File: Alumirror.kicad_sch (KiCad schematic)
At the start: 26 parts, among them J1 USB_C_Receptacle_USB2.0_16P_2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, J3 USB_C_Receptacle_USB2.0_16P_2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, SW10 BOOT, U1 CH552T, U3 USBLC6-2P6, U5 USBLC6-2P6

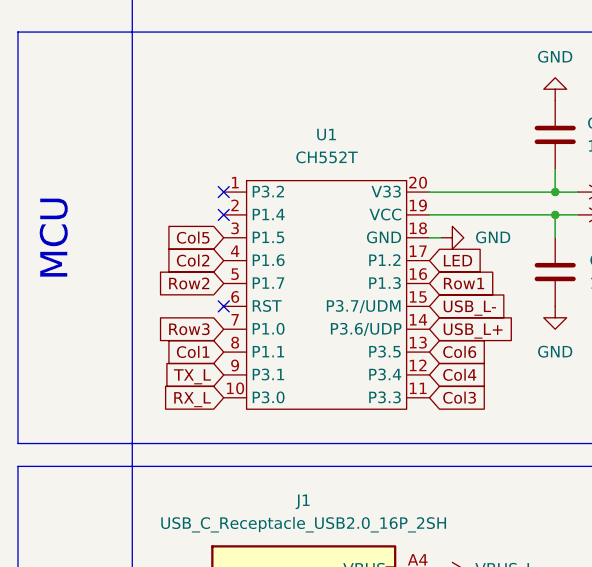
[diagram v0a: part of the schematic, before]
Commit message: Move thumb keys to new Row 4
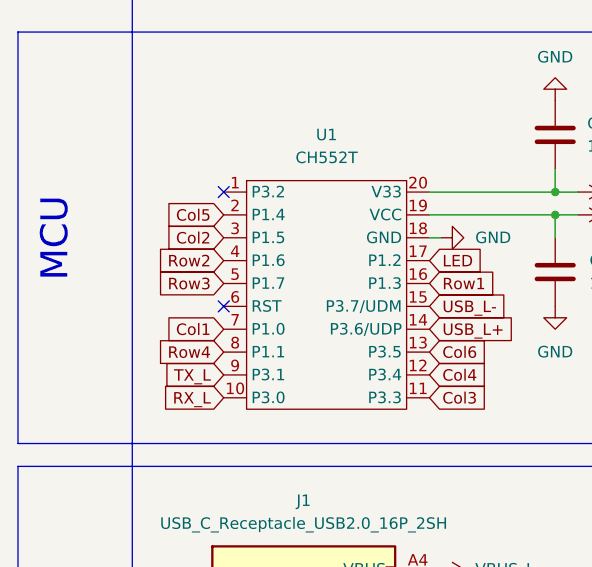
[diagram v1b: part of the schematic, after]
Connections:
- net Col1: now also U1.7 (P1.0); no longer U1.8 (P1.1)
- net Col2: now also U1.3 (P1.5); no longer U1.4 (P1.6)
- net Col5: now also U1.2 (P1.4); no longer U1.3 (P1.5)
- net Row2: now also U1.4 (P1.6); no longer U1.5 (P1.7)
- net Row3: now also U1.5 (P1.7); no longer U1.7 (P1.0)
- new net Row4: U1.8 (P1.1)
- no-connect marks 17 -> 16

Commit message: Various tweaks
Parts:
- removed R7: 0R, Resistor_SMD:R_2010_5025Metric, symbol Device:R
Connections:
- net VCC_L' is gone; now on net VCC_L: J3.A4 (VBUS), J3.A9 (VBUS), J3.B4 (VBUS), J3.B9 (VBUS), U5.5 (VBUS)
- net Col1: now also U1.4 (P1.6); no longer U1.7 (P1.0)
- net Col3: now also U1.2 (P1.4); no longer U1.11 (P3.3)
- net Col5: now also U1.11 (P3.3); no longer U1.2 (P1.4)
- net Row2: now also U1.5 (P1.7); no longer U1.4 (P1.6)
- net Row3: now also U1.7 (P1.0); no longer U1.5 (P1.7)
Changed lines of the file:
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@@
 	(global_label "Col1"
 		(shape input)
-		(at 38.1 58.42 180)
+		(at 38.1 50.8 180)
 		(fields_autoplaced yes)
 		(effects
@@
 		)
 		(property "Intersheetrefs" "${INTERSHEET_REFS}"
-			(at 30.8211 58.42 0)
+			(at 30.8211 50.8 0)
 			(effects
 				(font
@@
 	(global_label "Row3"
 		(shape input)
-		(at 38.1 53.34 180)
+		(at 38.1 58.42 180)
 		(fields_autoplaced yes)
 		(effects
@@
 		)
 		(property "Intersheetrefs" "${INTERSHEET_REFS}"
-			(at 30.1558 53.34 0)
+			(at 30.1558 58.42 0)
 			(effects
 				(font
@@
 	(global_label "Row2"
 		(shape input)
-		(at 38.1 50.8 180)
+		(at 38.1 53.34 180)
 		(fields_autoplaced yes)
 		(effects
@@
 		)
 		(property "Intersheetrefs" "${INTERSHEET_REFS}"
-			(at 30.1558 50.8 0)
+			(at 30.1558 53.34 0)
 			(effects
 				(font
@@
 		)
 	)
-	(global_label "Col5"
+	(global_label "Col3"
 		(shape input)
 		(at 38.1 45.72 180)
@@
 		)
 	)
-	(global_label "Col3"
+	(global_label "Col5"
 		(shape input)
 		(at 60.96 66.04 0)
@@
 			)
 		)
-		(property "Value" "VCC_L'"
+		(property "Value" "VCC_L"
 			(at 66.04 151.1299 90)
 			(effects
@@
 			)
 		)
-		(property "Value" "VCC_L'"
+		(property "Value" "VCC_L"
 			(at 120.65 168.91 0)
 			(effects
@@
 	)
 	(symbol
-		(lib_id "power:VCC")
-		(at 124.46 157.48 270)
-		(unit 1)
-		(exclude_from_sim no)
-		(in_bom yes)
-		(on_board yes)
-		(dnp no)
-		(fields_autoplaced yes)
-		(property "Reference" "#PWR019"
-			(at 120.65 157.48 0)
-			(effects
-				(font
-					(size 1.27 1.27)
-				)
-				(hide yes)
-			)
-		)
-		(property "Value" "VCC_L'"
-			(at 128.27 157.4799 90)
-			(effects
-				(font
-					(size 1.27 1.27)
-				)
-				(justify left)
-			)
-		)
-		(property "Footprint" ""
-			(at 124.46 157.48 0)
-			(effects
-				(font
-					(size 1.27 1.27)
-				)
-				(hide yes)
-			)
-		)
-		(property "Datasheet" ""
-			(at 124.46 157.48 0)
-			(effects
-				(font
-					(size 1.27 1.27)
-				)
-				(hide yes)
-			)
-		)
-		(property "Description" ""
-			(at 124.46 157.48 0)
-			(effects
-				(font
-					(size 1.27 1.27)
-				)
-				(hide yes)
-			)
-		)
-		(pin "1"
-		)
-		(instances
-			(project "Alumirror"
-				(path "/52f043ac-ccff-4c85-bc10-2db9d3c9e3f3"
-					(reference "#PWR019")
-					(unit 1)
-				)
-			)
-		)
-	)
-	(symbol
 		(lib_id "power:GND")
 		(at 120.65 120.65 0)
@@
 	)
 	(symbol
-		(lib_id "Device:R")
-		(at 120.65 157.48 90)
-		(unit 1)
-		(exclude_from_sim no)
-		(in_bom yes)
-		(on_board yes)
-		(dnp no)
-		(fields_autoplaced yes)
-		(property "Reference" "R7"
-			(at 120.65 151.13 90)
-			(effects
-				(font
-					(size 1.27 1.27)
-				)
-			)
-		)
-		(property "Value" "0R"
-			(at 120.65 153.67 90)
-			(effects
-				(font
-					(size 1.27 1.27)
-				)
-			)
-		)
-		(property "Footprint" "Resistor_SMD:R_2010_5025Metric"
-			(at 120.65 159.258 90)
-			(effects
-				(font
-					(size 1.27 1.27)
-				)
-				(hide yes)
-			)
-		)
-		(property "Datasheet" "~"
-			(at 120.65 157.48 0)
-			(effects
-				(font
-					(size 1.27 1.27)
-				)
-				(hide yes)
-			)
-		)
-		(property "Description" "Resistor"
-			(at 120.65 157.48 0)
-			(effects
-				(font
-					(size 1.27 1.27)
-				)
-				(hide yes)
-			)
-		)
-		(pin "1"
-		)
-		(pin "2"
-		)
-		(instances
-			(project "Alumirror"
-				(path "/52f043ac-ccff-4c85-bc10-2db9d3c9e3f3"
-					(reference "R7")
-					(unit 1)
-				)
-			)
-		)
-	)
-	(symbol
 		(lib_id "Mechanical:MountingHole")
 		(at 254 270.51 0)
@@
 					(unit 1)
 				)
-			)
-		)
-	)
-	(symbol
-		(lib_id "power:VCC")
-		(at 116.84 157.48 90)
-		(unit 1)
-		(exclude_from_sim no)
-		(in_bom yes)
-		(on_board yes)
-		(dnp no)
-		(fields_autoplaced yes)
-		(property "Reference" "#PWR018"
-			(at 120.65 157.48 0)
-			(effects
-				(font
-					(size 1.27 1.27)
-				)
-				(hide yes)
-			)
-		)
-		(property "Value" "VCC_L"
-			(at 113.03 157.4799 90)
-			(effects
-				(font
-					(size 1.27 1.27)
-				)
-				(justify left)
-			)
-		)
-		(property "Footprint" ""
-			(at 116.84 157.48 0)
-			(effects
-				(font
-					(size 1.27 1.27)
-				)
-				(hide yes)
-			)
-		)
-		(property "Datasheet" ""
-			(at 116.84 157.48 0)
-			(effects
-				(font
-					(size 1.27 1.27)
-				)
-				(hide yes)
-			)
-		)
-		(property "Description" ""
-			(at 116.84 157.48 0)
-			(effects
-				(font
-					(size 1.27 1.27)
-				)
-				(hide yes)
-			)
-		)
-		(pin "1"
-		)
-		(instances
-			(project "Alumirror"
-				(path "/52f043ac-ccff-4c85-bc10-2db9d3c9e3f3"
-					(reference "#PWR018")
-					(unit 1)
-				)
